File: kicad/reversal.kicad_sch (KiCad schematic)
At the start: 27 parts, among them J1 USB_A

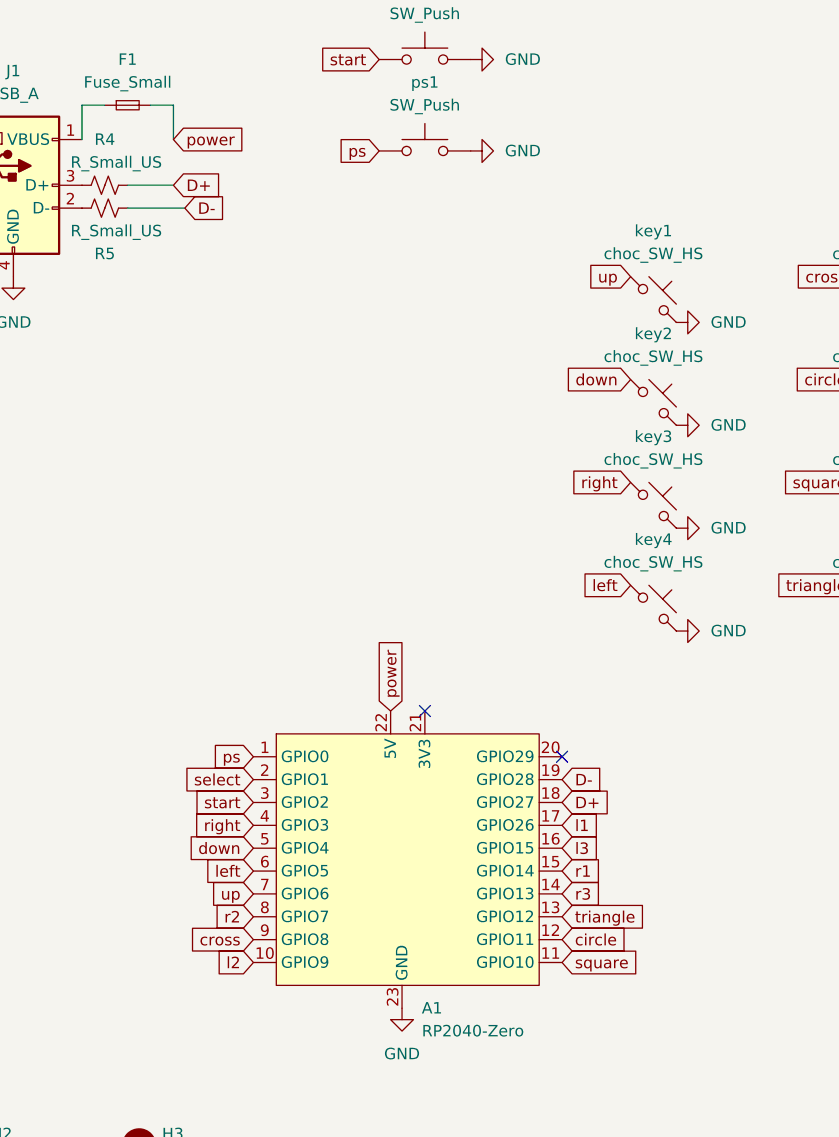
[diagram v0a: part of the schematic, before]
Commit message: Added touch button & rerouted traces to accomodate
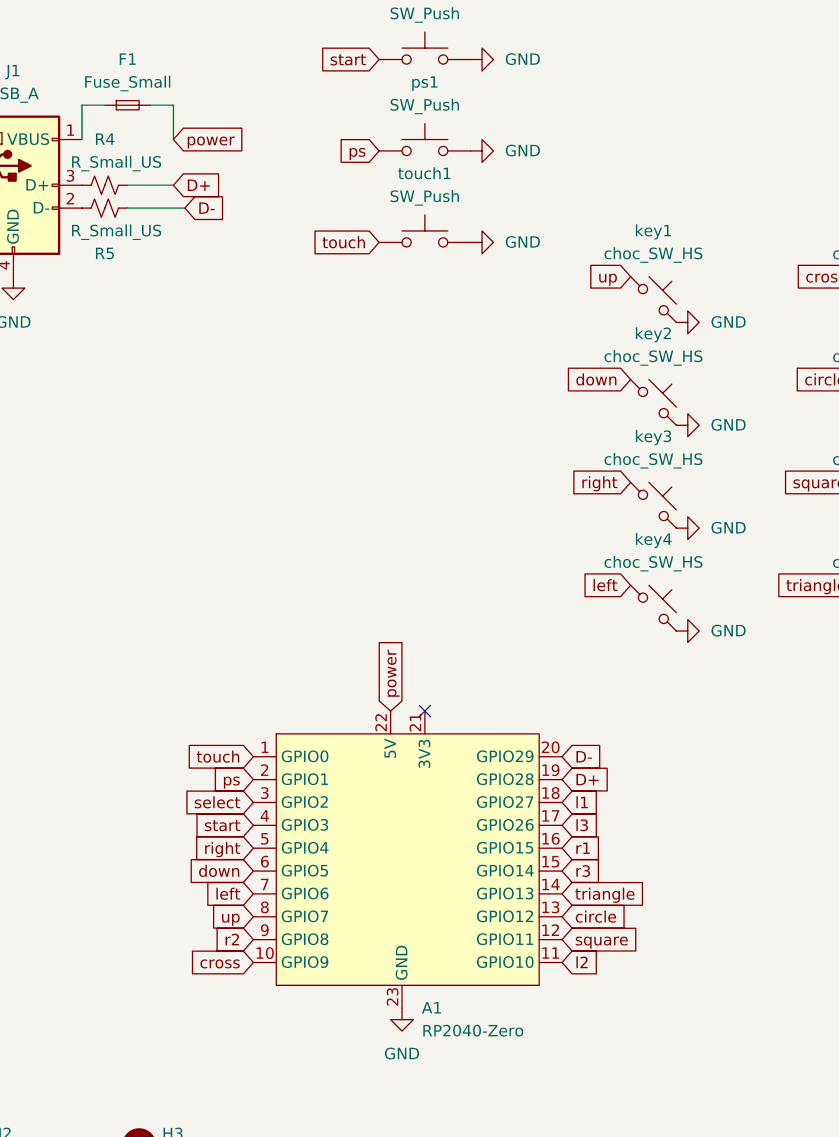
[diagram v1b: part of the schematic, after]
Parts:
- added touch1: SW_Push, Button_Switch_THT:SW_PUSH_6mm, symbol Switch:SW_Push
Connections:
- net D+: now also A1.19 (GPIO28); no longer A1.18 (GPIO27)
- net D-: now also A1.20 (GPIO29); no longer A1.19 (GPIO28)
- net GND: now also touch1.2
- net circle: now also A1.13 (GPIO12); no longer A1.12 (GPIO11)
- net cross: now also A1.10 (GPIO9); no longer A1.9 (GPIO8)
- net down: now also A1.6 (GPIO5); no longer A1.5 (GPIO4)
- net l1: now also A1.18 (GPIO27); no longer A1.17 (GPIO26)
- net l2: now also A1.11 (GPIO10); no longer A1.10 (GPIO9)
- net l3: now also A1.17 (GPIO26); no longer A1.16 (GPIO15)
- net left: now also A1.7 (GPIO6); no longer A1.6 (GPIO5)
- net ps: now also A1.2 (GPIO1); no longer A1.1 (GPIO0)
- net r1: now also A1.16 (GPIO15); no longer A1.15 (GPIO14)
- net r2: now also A1.9 (GPIO8); no longer A1.8 (GPIO7)
- net r3: now also A1.15 (GPIO14); no longer A1.14 (GPIO13)
- net right: now also A1.5 (GPIO4); no longer A1.4 (GPIO3)
- net select: now also A1.3 (GPIO2); no longer A1.2 (GPIO1)
- net square: now also A1.12 (GPIO11); no longer A1.11 (GPIO10)
- net start: now also A1.4 (GPIO3); no longer A1.3 (GPIO2)
- net triangle: now also A1.14 (GPIO13); no longer A1.13 (GPIO12)
- net up: now also A1.8 (GPIO7); no longer A1.7 (GPIO6)
- new net touch: A1.1 (GPIO0), touch1.1
- no-connect marks 3 -> 2

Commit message: Fixed library linking issues
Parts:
- J1: footprint Southpaw:USB_A_Female_C42425 -> Reversal:USB_A_Female_C42425
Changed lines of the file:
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@@
       (effects (font (size 1.27 1.27)))
     )
-    (property "Footprint" "Southpaw:USB_A_Female_C42425" (at 49.53 66.04 0)
+    (property "Footprint" "Reversal:USB_A_Female_C42425" (at 49.53 66.04 0)
       (effects (font (size 1.27 1.27)) hide)
     )
